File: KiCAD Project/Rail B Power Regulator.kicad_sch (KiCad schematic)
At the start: 11 parts, among them U1 TPS62130RGTR

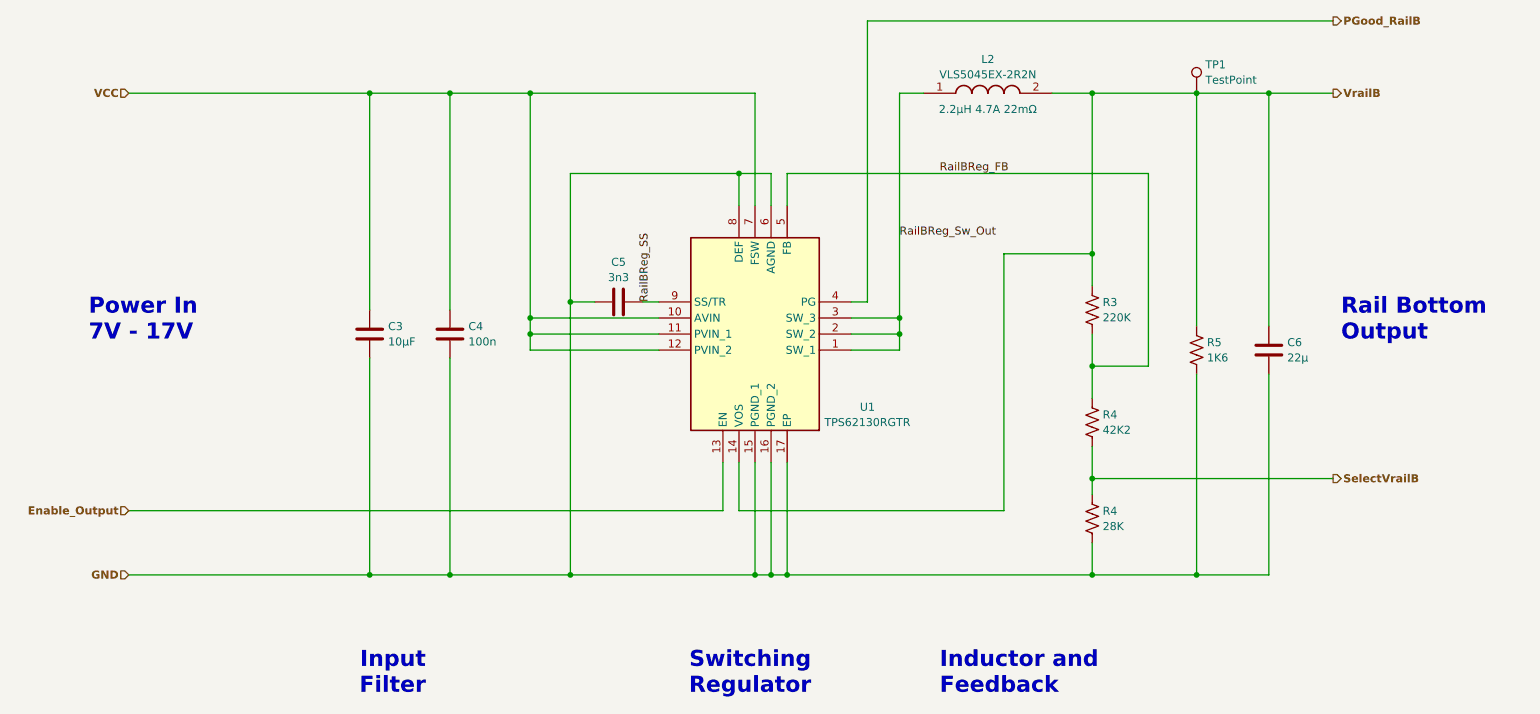
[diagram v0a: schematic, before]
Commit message: v2.0.0.0
1016 Breadboard Power Supply v2

- Change FSW connection to the Vout on all regulators
- Change regulator to TPS62130A so that PG pin goes low on thermal shutdown and UVLO
- Change PG pullup to be a resistor at the regulator vice pullup within STM32 so that it can be actively discharged
- Remove resistor across rail outputs for discharging to improve efficiency
- Change board dimensions to correct span
- Change pinout of STM32 for better routing
- Change Tag-Connect footprint to momentary connection (no legs)
- Make sure Tag-Connect footprint doesn't have solder paste layer
- Added heat sinks on bottom under rail regulators, added thermal vias
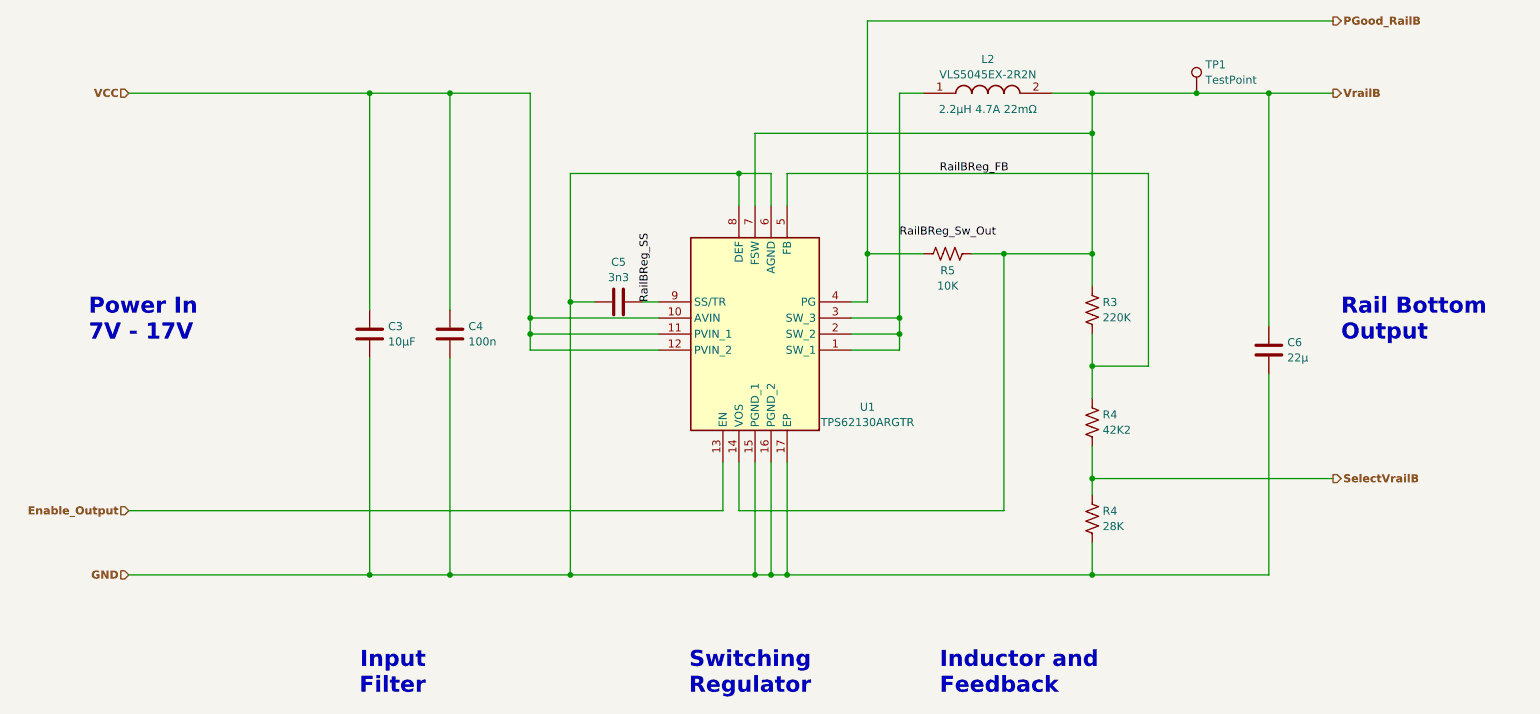
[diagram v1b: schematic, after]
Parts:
- R5: value 1K6 -> 10K; LCSC Part Number C165489 -> C98220; Manufacturer_Part_Number RC0603FR-071K6L -> RC0603FR-0710KL; Mouser Part Number 603-RC0603FR-071K6L -> 603-RC0603FR-0710KL; Spec 1K6 100mW -> 10K 100mW
- U1: value TPS62130RGTR -> TPS62130ARGTR; LCSC Part Number C43590 -> C337502; Manufacturer_Part_Number TPS62130RGTR -> TPS62130ARGTR; Mouser Part Number 595-TPS62130RGTR -> 595-TPS62130ARGTR
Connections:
- net GND: no longer R5.1
- net PGood_RailB: now also R5.2
- net VCC: no longer U1.7 (FSW)
- net VrailB: now also R5.1, U1.7 (FSW); no longer R5.2
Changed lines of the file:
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@@
     (comment 1 "Copyright © 2023, Dan Wilson")
   )
+  (junction (at 185.42 82.55) (diameter 0) (color 0 0 0 0)
+  )
   (junction (at 227.33 57.15) (diameter 0) (color 0 0 0 0)
   )
@@
   (junction (at 199.39 57.15) (diameter 0) (color 0 0 0 0)
   )
-  (junction (at 110.49 57.15) (diameter 0) (color 0 0 0 0)
-  )
   (junction (at 215.9 57.15) (diameter 0) (color 0 0 0 0)
   )
@@
   (junction (at 168.91 92.71) (diameter 0) (color 0 0 0 0)
   )
+  (junction (at 199.39 63.5) (diameter 0) (color 0 0 0 0)
+  )
   (junction (at 97.79 133.35) (diameter 0) (color 0 0 0 0)
   )
@@
   (junction (at 148.59 133.35) (diameter 0) (color 0 0 0 0)
   )
-  (junction (at 215.9 133.35) (diameter 0) (color 0 0 0 0)
-  )
   (junction (at 199.39 133.35) (diameter 0) (color 0 0 0 0)
   )
@@
   (junction (at 151.13 133.35) (diameter 0) (color 0 0 0 0)
   )
+  (junction (at 163.83 82.55) (diameter 0) (color 0 0 0 0)
+  )
   (wire (pts (xy 128.27 90.17) (xy 130.81 90.17))
     (stroke (width 0) (type default))
@@
     (stroke (width 0) (type default))
   )
-  (wire (pts (xy 146.05 74.93) (xy 146.05 57.15))
-    (stroke (width 0) (type default))
-  )
-  (wire (pts (xy 146.05 57.15) (xy 110.49 57.15))
+  (wire (pts (xy 146.05 74.93) (xy 146.05 63.5))
     (stroke (width 0) (type default))
   )
@@
     (stroke (width 0) (type default))
   )
+  (wire (pts (xy 180.34 82.55) (xy 185.42 82.55))
+    (stroke (width 0) (type default))
+  )
   (wire (pts (xy 168.91 95.25) (xy 168.91 97.79))
     (stroke (width 0) (type default))
@@
     (stroke (width 0) (type default))
   )
-  (wire (pts (xy 163.83 45.72) (xy 163.83 90.17))
+  (wire (pts (xy 163.83 45.72) (xy 163.83 82.55))
+    (stroke (width 0) (type default))
+  )
+  (wire (pts (xy 199.39 63.5) (xy 199.39 82.55))
     (stroke (width 0) (type default))
   )
@@
     (stroke (width 0) (type default))
   )
-  (wire (pts (xy 215.9 57.15) (xy 215.9 93.98))
-    (stroke (width 0) (type default))
-  )
   (wire (pts (xy 151.13 133.35) (xy 151.13 115.57))
     (stroke (width 0) (type default))
@@
     (stroke (width 0) (type default))
   )
-  (wire (pts (xy 215.9 101.6) (xy 215.9 133.35))
-    (stroke (width 0) (type default))
-  )
   (wire (pts (xy 193.04 57.15) (xy 199.39 57.15))
     (stroke (width 0) (type default))
@@
     (stroke (width 0) (type default))
   )
-  (wire (pts (xy 215.9 133.35) (xy 227.33 133.35))
-    (stroke (width 0) (type default))
-  )
   (wire (pts (xy 148.59 133.35) (xy 148.59 115.57))
     (stroke (width 0) (type default))
@@
     (stroke (width 0) (type default))
   )
-  (wire (pts (xy 199.39 57.15) (xy 199.39 82.55))
+  (wire (pts (xy 199.39 57.15) (xy 199.39 63.5))
     (stroke (width 0) (type default))
   )
@@
     (stroke (width 0) (type default))
   )
-  (wire (pts (xy 199.39 133.35) (xy 215.9 133.35))
+  (wire (pts (xy 199.39 133.35) (xy 227.33 133.35))
     (stroke (width 0) (type default))
   )
@@
     (stroke (width 0) (type default))
   )
+  (wire (pts (xy 146.05 63.5) (xy 199.39 63.5))
+    (stroke (width 0) (type default))
+  )
   (wire (pts (xy 148.59 133.35) (xy 151.13 133.35))
     (stroke (width 0) (type default))
@@
     (stroke (width 0) (type default))
   )
+  (wire (pts (xy 163.83 82.55) (xy 172.72 82.55))
+    (stroke (width 0) (type default))
+  )
   (wire (pts (xy 199.39 118.11) (xy 237.49 118.11))
     (stroke (width 0) (type default))
@@
   )
   (wire (pts (xy 199.39 82.55) (xy 199.39 87.63))
+    (stroke (width 0) (type default))
+  )
+  (wire (pts (xy 163.83 82.55) (xy 163.83 90.17))
     (stroke (width 0) (type default))
   )
@@
       (effects (font (size 1.27 1.27)))
     )
-    (property "Value" "TPS62130RGTR" (at 163.83 109.22 0)
+    (property "Value" "TPS62130ARGTR" (at 163.83 109.22 0)
       (effects (font (size 1.27 1.27)))
     )
@@
       (effects (font (size 1.27 1.27)) (justify left top) hide)
     )
-    (property "Manufacturer_Part_Number" "TPS62130RGTR" (at 134.62 -486.97 0)
-      (effects (font (size 1.27 1.27)) (justify left top) hide)
-    )
-    (property "Mouser Part Number" "595-TPS62130RGTR" (at 134.62 -586.97 0)
+    (property "Manufacturer_Part_Number" "TPS62130ARGTR" (at 134.62 -486.97 0)
+      (effects (font (size 1.27 1.27)) (justify left top) hide)
+    )
+    (property "Mouser Part Number" "595-TPS62130ARGTR" (at 134.62 -586.97 0)
       (effects (font (size 1.27 1.27)) (justify left top) hide)
     )
@@
       (effects (font (size 1.27 1.27)) hide)
     )
-    (property "LCSC Part Number" "C43590" (at 161.29 97.79 0)
+    (property "LCSC Part Number" "C337502" (at 161.29 97.79 0)
       (effects (font (size 1.27 1.27)) hide)
     )
@@
     )
   )
+  (symbol (lib_id "Device:R_US") (at 176.53 82.55 270) (unit 1)
+    (in_bom yes) (on_board yes) (dnp no)
+    (property "Reference" "R5" (at 176.53 85.2058 90)
+      (effects (font (size 1.27 1.27)))
+    )
+    (property "Value" "10K" (at 176.53 87.63 90)
+      (effects (font (size 1.27 1.27)))
+    )
+    (property "Footprint" "Resistor_SMD:R_0603_1608Metric" (at 176.276 83.566 90)
+      (effects (font (size 1.27 1.27)) hide)
+    )
+    (property "Datasheet" "https://www.mouser.com/datasheet/2/447/YAGEO_PYu_RC_Group_51_RoHS_L_12-3313492.pdf" (at 176.53 82.55 0)
+      (effects (font (size 1.27 1.27)) hide)
+    )
+    (property "Description" "Power Good Pull-Up Resistor" (at 176.53 82.55 0)
+      (effects (font (size 1.27 1.27)) hide)
+    )
+    (property "Height" "0.45" (at 176.53 82.55 0)
+      (effects (font (size 1.27 1.27)) hide)
+    )
+    (property "LCSC Part Number" "C98220" (at 176.53 82.55 0)
+      (effects (font (size 1.27 1.27)) hide)
+    )
+    (property "Manufacturer_Name" "Yageo" (at 176.53 82.55 0)
+      (effects (font (size 1.27 1.27)) hide)
+    )
+    (property "Manufacturer_Part_Number" "RC0603FR-0710KL" (at 176.53 82.55 0)
+      (effects (font (size 1.27 1.27)) hide)
+    )
+    (property "Mouser Part Number" "603-RC0603FR-0710KL" (at 176.53 82.55 0)
+      (effects (font (size 1.27 1.27)) hide)
+    )
+    (property "Spec" "10K 100mW" (at 176.53 82.55 0)
+      (effects (font (size 1.27 1.27)) hide)
+    )
+    (pin "1")
+    (pin "2")
+    (instances
+      (project "1016 Breadboard Power Supply"
+        (path "/f4b22203-0926-4e3a-b453-85f22789c08a/1995aaec-8535-485d-8210-75eb1f946442"
+          (reference "R5") (unit 1)
+        )
+        (path "/f4b22203-0926-4e3a-b453-85f22789c08a/db2e6b67-906b-4487-b3aa-e456085ef032"
+          (reference "R6") (unit 1)
+        )
+      )
+    )
+  )
   (symbol (lib_id "1016:VLS5045EX-2R2N") (at 172.72 57.15 0) (unit 1)
     (in_bom yes) (on_board yes) (dnp no)
@@
         )
       )
-    )
-  )
-  (symbol (lib_id "Device:R_US") (at 215.9 97.79 180) (unit 1)
-    (in_bom yes) (on_board yes) (dnp no) (fields_autoplaced)
-    (property "Reference" "R5" (at 217.551 96.5779 0)
-      (effects (font (size 1.27 1.27)) (justify right))
-    )
-    (property "Value" "1K6" (at 217.551 99.0021 0)
-      (effects (font (size 1.27 1.27)) (justify right))
-    )
-    (property "Footprint" "Resistor_SMD:R_0603_1608Metric" (at 214.884 97.536 90)
-      (effects (font (size 1.27 1.27)) hide)
-    )
-    (property "Datasheet" "https://www.mouser.com/datasheet/2/447/YAGEO_PYu_RC_Group_51_RoHS_L_12-3313492.pdf" (at 215.9 97.79 0)
-      (effects (font (size 1.27 1.27)) hide)
-    )
-    (property "Description" "Output Discharge Resistor" (at 215.9 97.79 0)
-      (effects (font (size 1.27 1.27)) hide)
-    )
-    (property "Height" "0.45" (at 215.9 97.79 0)
-      (effects (font (size 1.27 1.27)) hide)
-    )
-    (property "LCSC Part Number" "C165489" (at 215.9 97.79 0)
-      (effects (font (size 1.27 1.27)) hide)
-    )
-    (property "Manufacturer_Name" "Yageo" (at 215.9 97.79 0)
-      (effects (font (size 1.27 1.27)) hide)
-    )
-    (property "Manufacturer_Part_Number" "RC0603FR-071K6L" (at 215.9 97.79 0)
-      (effects (font (size 1.27 1.27)) hide)
-    )
-    (property "Mouser Part Number" "603-RC0603FR-071K6L" (at 215.9 97.79 0)
-      (effects (font (size 1.27 1.27)) hide)
-    )
-    (property "Spec" "1K6 100mW" (at 215.9 97.79 0)
-      (effects (font (size 1.27 1.27)) hide)
-    )
-    (pin "1")
-    (pin "2")
-    (instances
-      (project "1016 Breadboard Power Supply"
-        (path "/f4b22203-0926-4e3a-b453-85f22789c08a/280adcb7-ede6-4688-bc7e-541657c4a091"
-          (reference "R5") (unit 1)
-        )
-        (path "/f4b22203-0926-4e3a-b453-85f22789c08a/1995aaec-8535-485d-8210-75eb1f946442"
-          (reference "R6") (unit 1)
-        )
-        (path "/f4b22203-0926-4e3a-b453-85f22789c08a/db2e6b67-906b-4487-b3aa-e456085ef032"
-          (reference "R10") (unit 1)
-        )
-      )
